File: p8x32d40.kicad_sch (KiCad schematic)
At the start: 14 parts, among them Q1 2N3904, SW1 SW_Push, U1 24LC512, U2 P8X32A-D40, Y1 5MHz

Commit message: [WIP] usb connector + ft232RNL
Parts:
- U2: renamed from U1; value 24LC512 -> M24512E-FMN6TP; footprint (none) -> Package_SO:SO-8_3.9x4.9mm_P1.27mm
- renumbered U2 to U1
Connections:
- net GND: no longer U2.1 (A0), U2.2 (A1), U2.3 (A2)
- no-connect marks 0 -> 3
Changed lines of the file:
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@@
   (junction (at 35.56 167.64) (diameter 0) (color 0 0 0 0)
   )
-  (junction (at 221.615 62.23) (diameter 0) (color 0 0 0 0)
-  )
   (junction (at 52.705 30.48) (diameter 0) (color 0 0 0 0)
   )
@@
   (junction (at 52.705 95.25) (diameter 0) (color 0 0 0 0)
   )
-  (junction (at 221.615 64.77) (diameter 0) (color 0 0 0 0)
-  )
+  (no_connect (at 219.075 59.69))
+  (no_connect (at 219.075 64.77))
+  (no_connect (at 219.075 62.23))
   (polyline (pts (xy 231.775 18.415) (xy 272.415 18.415))
     (stroke (width 0) (type default))
@@
     (stroke (width 0) (type default))
   )
-  (wire (pts (xy 219.075 59.69) (xy 221.615 59.69))
-    (stroke (width 0) (type default))
-  )
   (wire (pts (xy 146.685 61.595) (xy 152.4 61.595))
     (stroke (width 0) (type default))
@@
     (stroke (width 0) (type default))
   )
-  (wire (pts (xy 221.615 62.23) (xy 221.615 64.77))
-    (stroke (width 0) (type default))
-  )
   (polyline (pts (xy 142.875 179.07) (xy 19.05 179.07))
     (stroke (width 0) (type default))
@@
     (stroke (width 0) (type default))
   )
-  (wire (pts (xy 221.615 64.77) (xy 221.615 69.85))
-    (stroke (width 0) (type default))
-  )
   (wire (pts (xy 35.56 140.97) (xy 35.56 144.145))
     (stroke (width 0) (type default))
@@
     (stroke (width 0) (type default))
   )
-  (wire (pts (xy 221.615 64.77) (xy 219.075 64.77))
-    (stroke (width 0) (type default))
-  )
   (wire (pts (xy 73.025 73.66) (xy 81.28 73.66))
     (stroke (width 0) (type default))
@@
     (stroke (width 0) (type default))
   )
-  (wire (pts (xy 221.615 59.69) (xy 221.615 62.23))
-    (stroke (width 0) (type default))
-  )
   (wire (pts (xy 29.21 50.8) (xy 37.465 50.8))
     (stroke (width 0) (type default))
@@
   )
   (polyline (pts (xy 182.245 18.415) (xy 95.885 18.415))
-    (stroke (width 0) (type default))
-  )
-  (wire (pts (xy 221.615 62.23) (xy 219.075 62.23))
     (stroke (width 0) (type default))
   )
@@
   (symbol (lib_id "Memory_EEPROM:24LC512") (at 208.915 62.23 0) (mirror y) (unit 1)
     (in_bom yes) (on_board yes) (dnp no) (fields_autoplaced)
-    (property "Reference" "U1" (at 206.7209 52.705 0)
-      (effects (font (size 1.27 1.27)) (justify left))
-    )
-    (property "Value" "24LC512" (at 206.7209 55.245 0)
-      (effects (font (size 1.27 1.27)) (justify left))
-    )
-    (property "Footprint" "" (at 208.915 62.23 0)
-      (effects (font (size 1.27 1.27)) hide)
-    )
-    (property "Datasheet" "http://ww1.microchip.com/downloads/en/DeviceDoc/21754M.pdf" (at 208.915 62.23 0)
+    (property "Reference" "U2" (at 206.7209 52.705 0)
+      (effects (font (size 1.27 1.27)) (justify left))
+    )
+    (property "Value" "M24512E-FMN6TP" (at 206.7209 55.245 0)
+      (effects (font (size 1.27 1.27)) (justify left))
+    )
+    (property "Footprint" "Package_SO:SO-8_3.9x4.9mm_P1.27mm" (at 208.915 62.23 0)
+      (effects (font (size 1.27 1.27)) hide)
+    )
+    (property "Datasheet" "https://www.st.com/resource/en/datasheet/m24512e-f.pdf" (at 208.915 62.23 0)
       (effects (font (size 1.27 1.27)) hide)
     )
@@
       (project "JTAGFinder"
         (path "/204d557f-3c83-43db-b1fd-628e15efe3d8/56d043b9-8fe6-4689-a732-ed49fd9c64ac"
-          (reference "U1") (unit 1)
+          (reference "U2") (unit 1)
         )
       )
@@
   (symbol (lib_id "MCU_Parallax:P8X32A-D40") (at 55.245 63.5 0) (unit 1)
     (in_bom yes) (on_board yes) (dnp no) (fields_autoplaced)
-    (property "Reference" "U2" (at 57.4391 34.925 0)
+    (property "Reference" "U1" (at 57.4391 34.925 0)
       (effects (font (size 1.27 1.27)) (justify left))
     )
@@
       (project "JTAGFinder"
         (path "/204d557f-3c83-43db-b1fd-628e15efe3d8/56d043b9-8fe6-4689-a732-ed49fd9c64ac"
-          (reference "U2") (unit 1)
+          (reference "U1") (unit 1)
         )
       )
@@
         )
       )
-    )
-  )
-  (symbol (lib_id "power:GND") (at 221.615 69.85 0) (mirror y) (unit 1)
-    (in_bom yes) (on_board yes) (dnp no) (fields_autoplaced)
-    (property "Reference" "#PWR016" (at 221.615 76.2 0)
-      (effects (font (size 1.27 1.27)) hide)
-    )
-    (property "Value" "GND" (at 221.615 74.295 0)
-      (effects (font (size 1.27 1.27)))
-    )
-    (property "Footprint" "" (at 221.615 69.85 0)
-      (effects (font (size 1.27 1.27)) hide)
-    )
-    (property "Datasheet" "" (at 221.615 69.85 0)
-      (effects (font (size 1.27 1.27)) hide)
-    )
-    (pin "1")
-    (instances
-      (project "JTAGFinder"
-        (path "/204d557f-3c83-43db-b1fd-628e15efe3d8/56d043b9-8fe6-4689-a732-ed49fd9c64ac"
-          (reference "#PWR016") (unit 1)
-        )
-      )

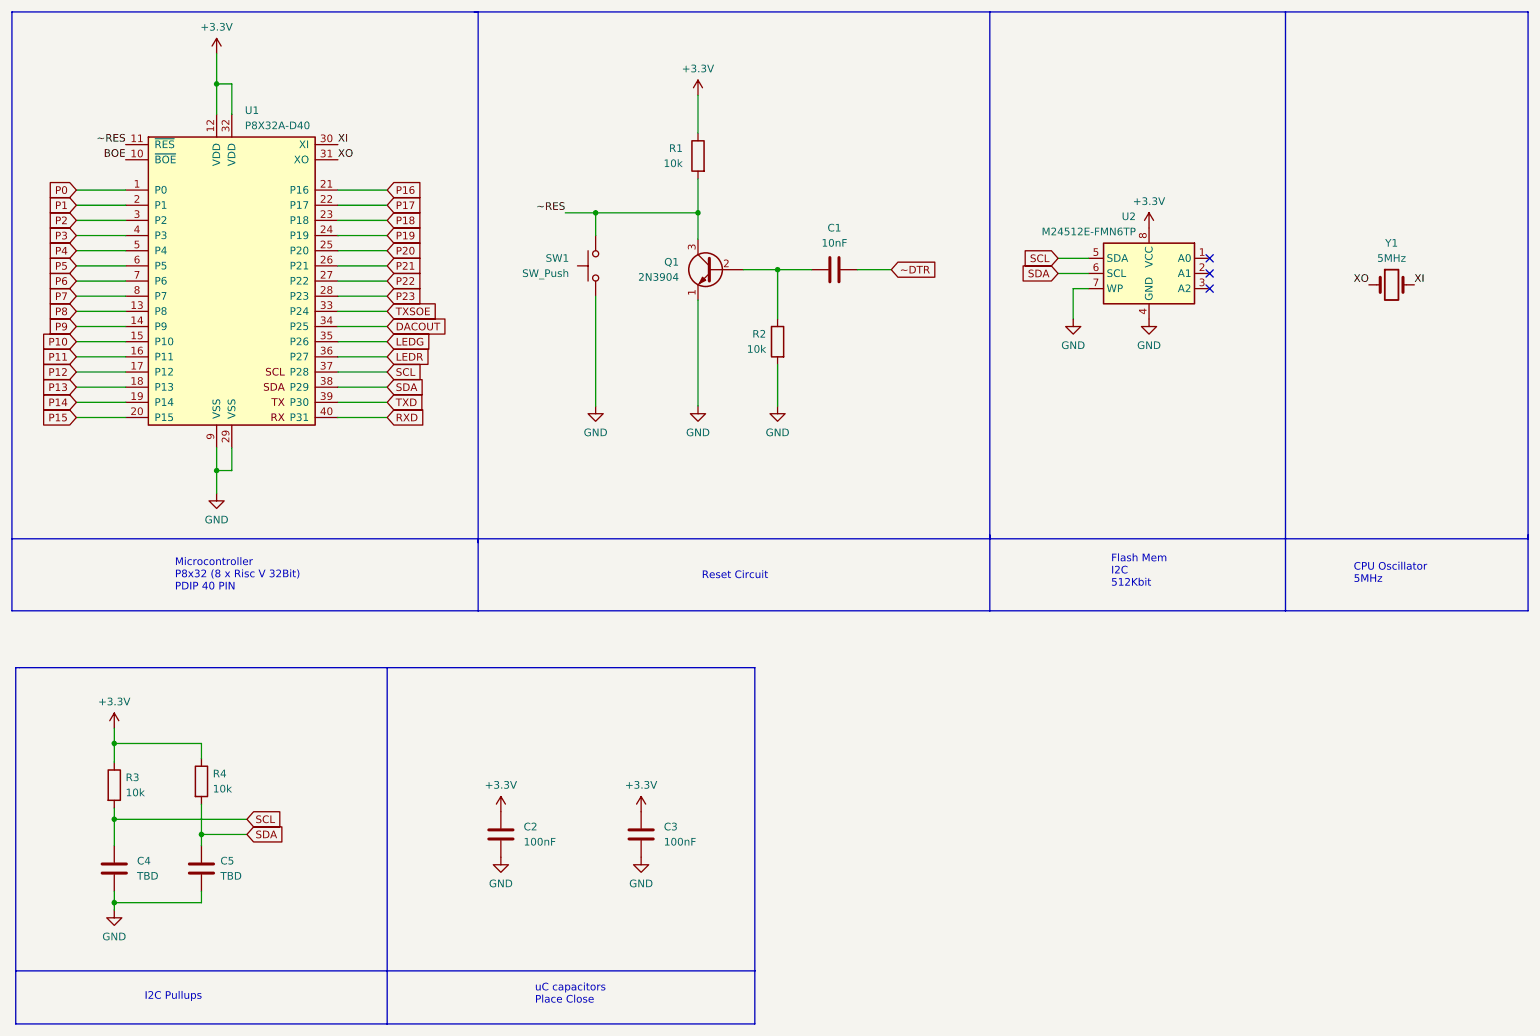
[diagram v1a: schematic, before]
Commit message: [FIX] ERC failure, add sheets for output stage
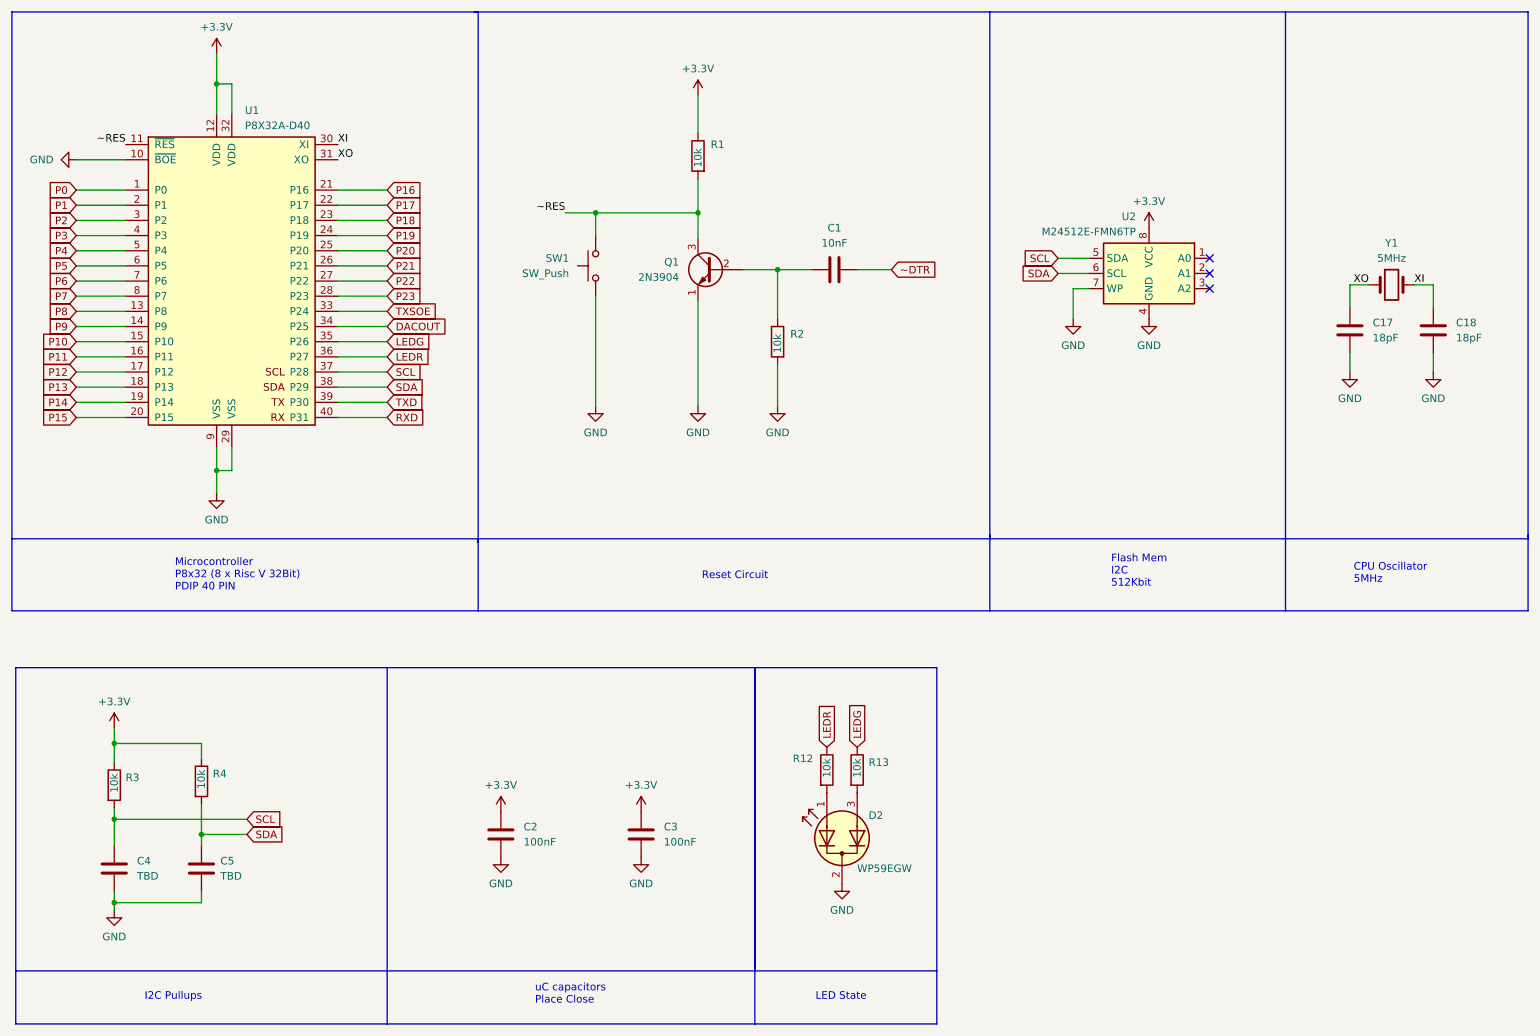
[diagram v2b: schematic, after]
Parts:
- added C17, C18: 18pF, symbol Device:C
- added D2: WP59EGW, symbol Device:LED_Dual_AKA
- added R12, R13: 10k, symbol Device:R
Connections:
- net BOE is gone; now on net GND: U1.10 (~{BOE})
- net GND: now also C17.2, C18.2, D2.2 (K)
- net LEDG: now also R13.1
- net LEDR: now also R12.1
- net XI: now also C18.1
- net XO: now also C17.1
- new net: D2.1 (A1), R12.2
- new net: D2.3 (A2), R13.2
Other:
- note added: "LED State"

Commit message: [WIP] pcb design with minor fixes in schema to have cleanest routing
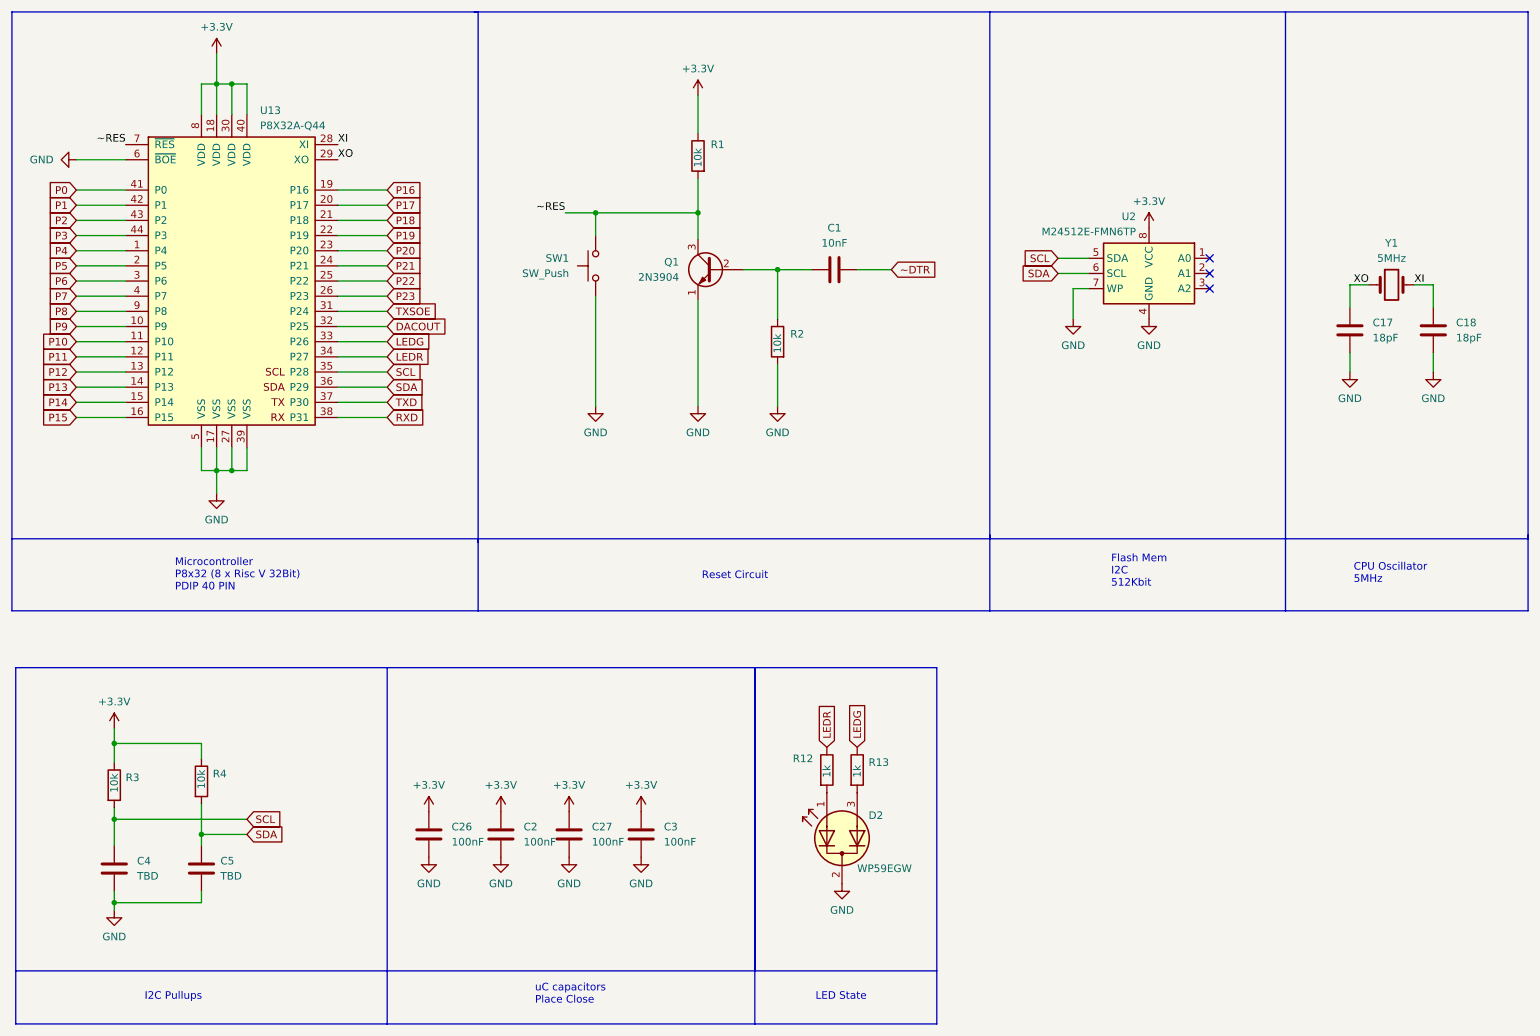
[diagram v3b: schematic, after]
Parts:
- removed U1: P8X32A-D40, Package_DIP:DIP-40_W15.24mm, symbol MCU_Parallax:P8X32A-D40
- added C26, C27: 100nF, Capacitor_SMD:C_1206_3216Metric, symbol Device:C
- added U13: P8X32A-Q44, Package_QFP:LQFP-44_10x10mm_P0.8mm, symbol MCU_Parallax:P8X32A-Q44
- C1: footprint (none) -> Capacitor_SMD:C_1206_3216Metric
- C17, C18: footprint (none) -> Capacitor_SMD:C_1206_3216Metric; Fab: (none) -> Yageo; Man #: (none) -> CC1206JRNPO9BN180
- C2, C3: footprint (none) -> Capacitor_SMD:C_1206_3216Metric; Fab: (none) -> Yageo; Man #: (none) -> CC1206KKX7RCBB103
- C4, C5: footprint (none) -> Capacitor_SMD:C_1206_3216Metric; Fab: (none) -> Walsin Tech Corp; Man #: (none) -> 1206B104K101CT
- D2: footprint (none) -> LED_THT:LED_D5.0mm-3; Fab: (none) -> KingBright; Man #: (none) -> WP59EGW/CA
- Q1: Fab: (none) -> JSMSEMI; Man #: (none) -> 2n3904
- R1, R2, R3, R4: footprint (none) -> Resistor_SMD:R_1206_3216Metric; Fab: (none) -> VO; Man #: (none) -> SCR1206J10K
- R12, R13: value 10k -> 1k; footprint (none) -> Resistor_SMD:R_1206_3216Metric; Fab: (none) -> VO; Man #: (none) -> SCR1206J10K
- SW1: footprint (none) -> Button_Switch_SMD:SW_SPST_PTS645; Fab: (none) -> ALPSALPINE; Man #: (none) -> SKQGADE010
- Y1: footprint (none) -> Crystal:Crystal_HC49-4H_Vertical
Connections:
- net  ~RES: now also U13.7 (~{RES})
- net +3.3V: now also C26.1, C27.1, U13.18 (VDD), U13.30 (VDD), U13.40 (VDD), U13.8 (VDD)
- net DACOUT: now also U13.32 (P25)
- net GND: now also C26.2, C27.2, U13.17 (VSS), U13.27 (VSS), U13.39 (VSS), U13.5 (VSS), U13.6 (~{BOE})
- net LEDG: now also U13.33 (P26)
- net LEDR: now also U13.34 (P27)
- net P0: now also U13.41 (P0)
- net P1: now also U13.42 (P1)
- net P10: now also U13.11 (P10)
- net P11: now also U13.12 (P11)
- net P12: now also U13.13 (P12)
- net P13: now also U13.14 (P13)
- net P14: now also U13.15 (P14)
- net P15: now also U13.16 (P15)
- net P16: now also U13.19 (P16)
- net P17: now also U13.20 (P17)
- net P18: now also U13.21 (P18)
- net P19: now also U13.22 (P19)
- net P2: now also U13.43 (P2)
- net P20: now also U13.23 (P20)
- net P21: now also U13.24 (P21)
- net P22: now also U13.25 (P22)
- net P23: now also U13.26 (P23)
- net P3: now also U13.44 (P3)
- net P4: now also U13.1 (P4)
- net P5: now also U13.2 (P5)
- net P6: now also U13.3 (P6)
- net P7: now also U13.4 (P7)
- net P8: now also U13.9 (P8)
- net P9: now also U13.10 (P9)
- net RXD: now also U13.38 (P31)
- net SCL: now also U13.35 (P28)
- net SDA: now also U13.36 (P29)
- net TXD: now also U13.37 (P30)
- net TXSOE: now also U13.31 (P24)
- net XI: now also U13.28 (XI)
- net XO: now also U13.29 (XO)

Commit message: finish update extra updates
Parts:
- SW1: footprint Button_Switch_SMD:SW_SPST_PTS645 -> Button_Switch_SMD:SW_SPST_CK_KXT3
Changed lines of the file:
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@@
       (effects (font (size 1.27 1.27)) (justify left))
     )
-    (property "Footprint" "Button_Switch_SMD:SW_SPST_PTS645" (at 111.125 60.96 0)
+    (property "Footprint" "Button_Switch_SMD:SW_SPST_CK_KXT3" (at 111.125 60.96 0)
       (effects (font (size 1.27 1.27)) hide)
     )

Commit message: update psu CI due thermal problems
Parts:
- SW1: footprint Button_Switch_SMD:SW_SPST_CK_KXT3 -> Button_Switch_SMD:SW_Push_1P1T_XKB_TS-1187A
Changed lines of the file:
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@@
       (effects (font (size 1.27 1.27)) (justify left))
     )
-    (property "Footprint" "Button_Switch_SMD:SW_SPST_CK_KXT3" (at 111.125 60.96 0)
+    (property "Footprint" "Button_Switch_SMD:SW_Push_1P1T_XKB_TS-1187A" (at 111.125 60.96 0)
       (effects (font (size 1.27 1.27)) hide)
     )
